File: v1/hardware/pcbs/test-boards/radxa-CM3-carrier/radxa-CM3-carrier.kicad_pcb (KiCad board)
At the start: 4 copper layers, 80 x 100 mm, 46 parts, among them CN1 MX250-3.5-12P-A-GY01-CU-A, CN2 MX250-3.5-12P-A-GY01-CU-A, J3 Conn_02x02_Odd_Even, U1 CM4102008, U11 TCAN1057AVDRQ1, U12 MCP2518FD-xQBB, Y1 C5261245

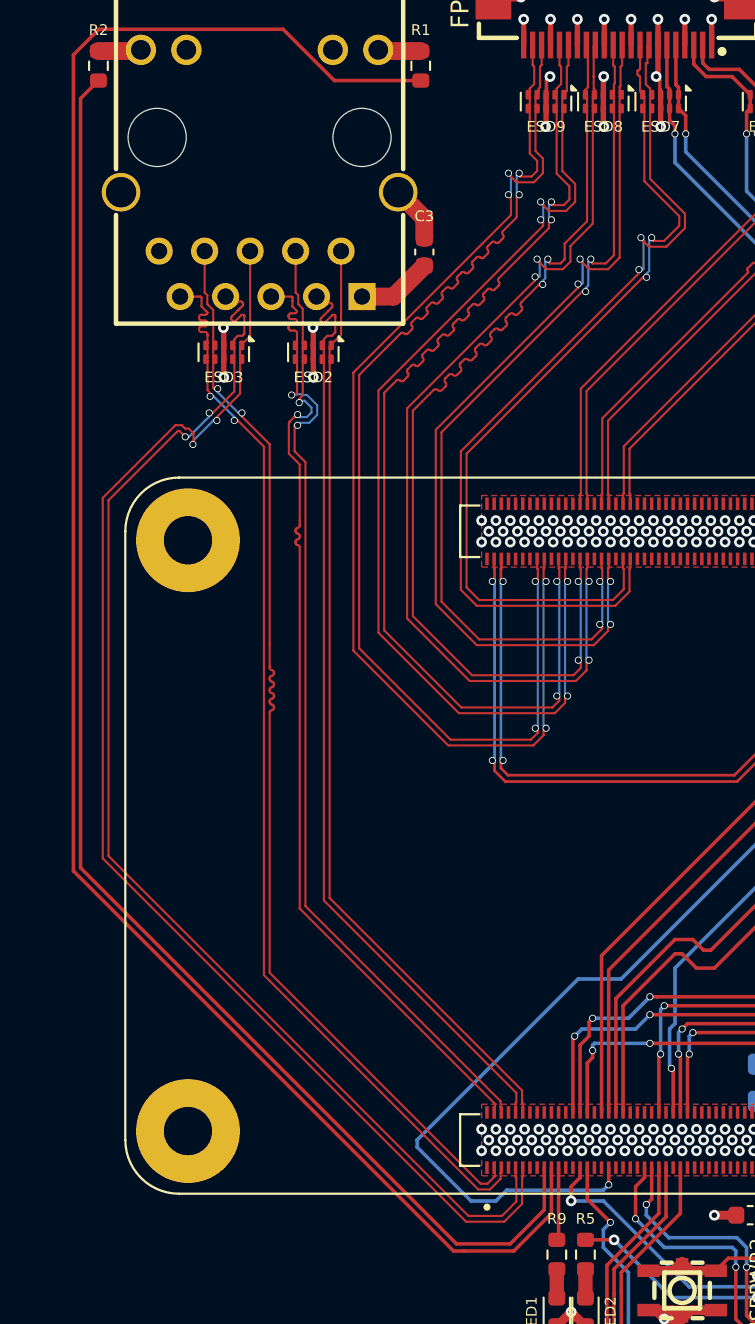
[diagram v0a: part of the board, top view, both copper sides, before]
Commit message: length matched differential pairs that i forgot
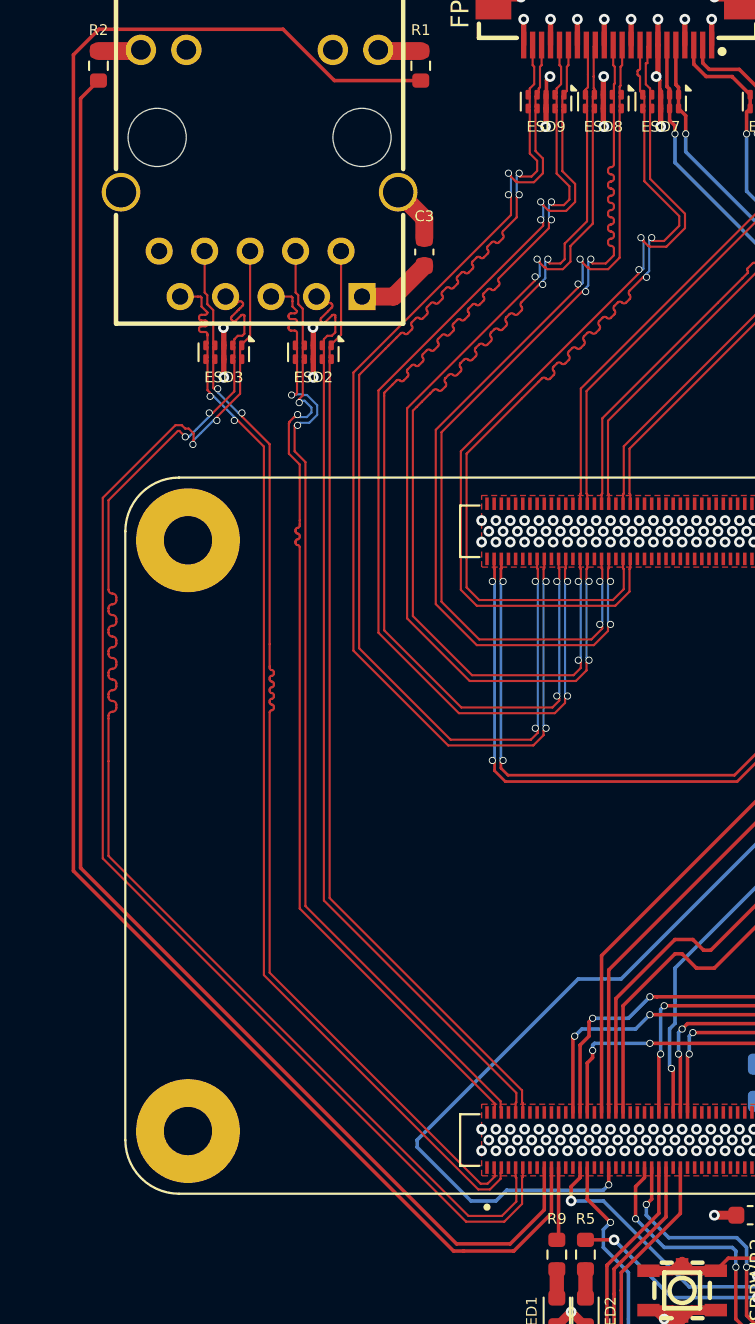
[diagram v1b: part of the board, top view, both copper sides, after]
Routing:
- net /ETH.D2-: track 71.3 -> 74.1 mm
- net /CAM1.D2-: track 50.6 -> 52.7 mm
- net /CAM1.D3-: track 48.2 -> 50.4 mm
